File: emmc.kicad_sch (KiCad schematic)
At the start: 16 parts, among them U22 HN8T05DEHK-X073

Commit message: Add files via upload
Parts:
- C320: renamed from C121; value 100n -> 1u
- C321: renamed from C122; value 100n -> 1u
- C322: renamed from C123; value 100n -> 1u
- C324: renamed from C129; value 100n -> 1u
- C325: renamed from C130; value 100n -> 1u
- C326: renamed from C131; value 100n -> 1u
- C331: renamed from C125; value 100n -> 1u
- C332: renamed from C126; value 100n -> 1u
- C333: renamed from C127; value 100n -> 1u
- renumbered C120 to C319, C128 to C323, C132 to C327, C133 to C328, C134 to C329, C124 to C330, U22 to U24
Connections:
- net +1.8V: no longer U24.A6 (VCCQ2), U24.A7 (VCCQ2), U24.B6 (VCCQ2), U24.B7 (VCCQ2), U24.C6 (VCCQ2), U24.C7 (VCCQ2), U24.K6 (VCCQ2), U24.K7 (VCCQ2)
- new net VCCQ2: U24.A6 (VCCQ2), U24.A7 (VCCQ2), U24.B6 (VCCQ2), U24.B7 (VCCQ2), U24.C6 (VCCQ2), U24.C7 (VCCQ2), U24.K6 (VCCQ2), U24.K7 (VCCQ2)
- no-connect marks 14 -> 15
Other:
- note added: "I NEED 2.5V & 1.2V"

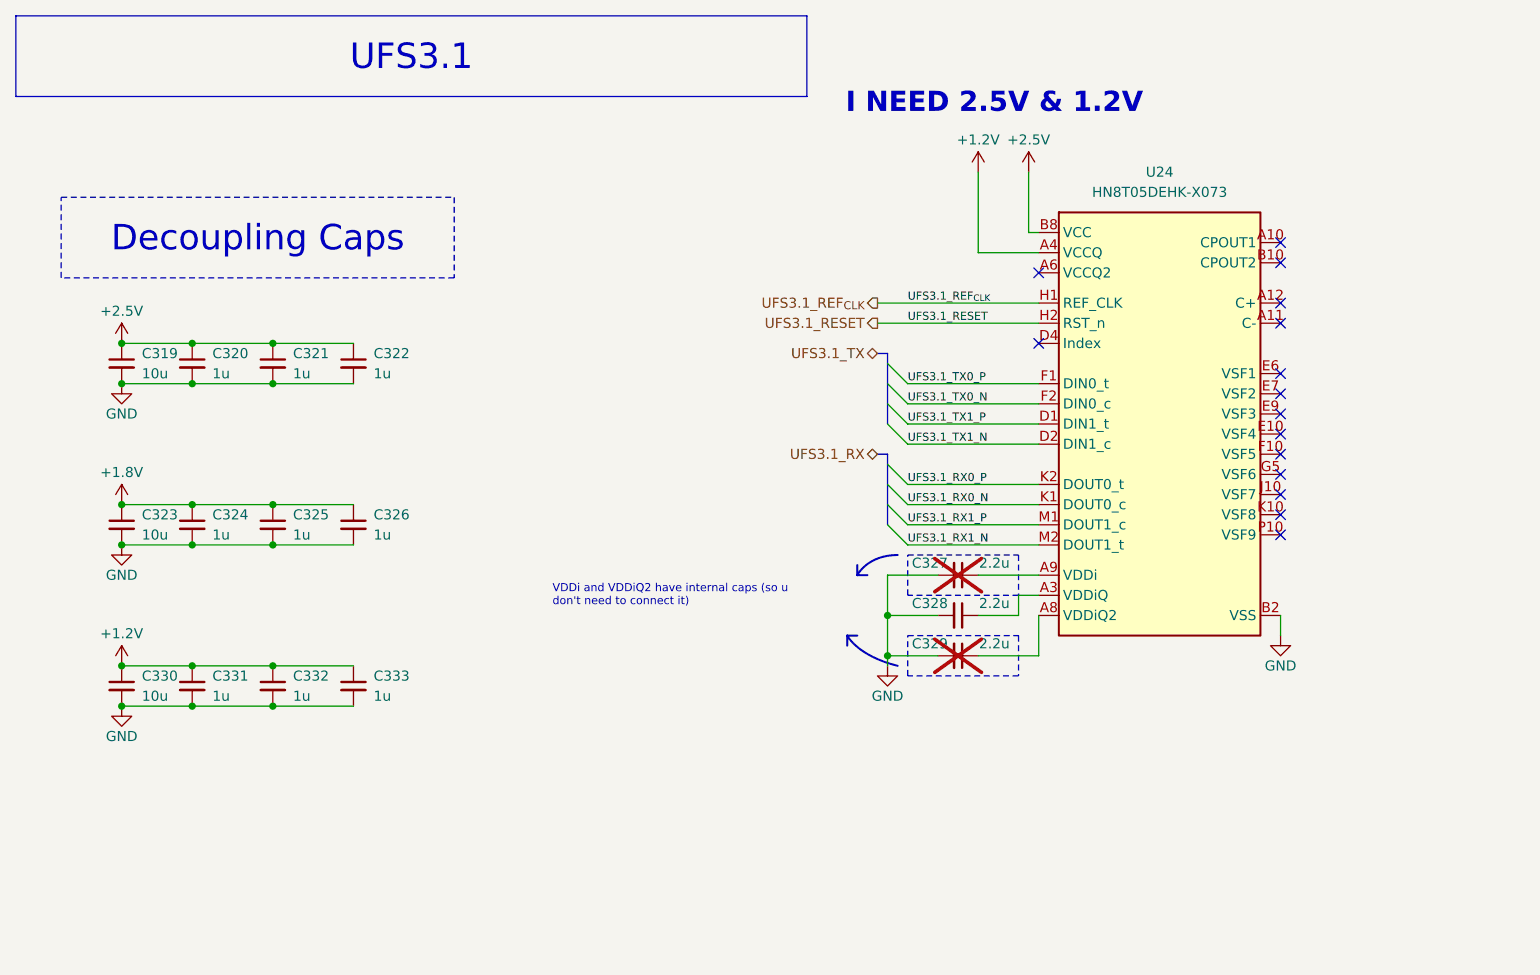
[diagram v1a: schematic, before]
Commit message: SBC Board V0.2
The SBC schematics before footprint and part number check
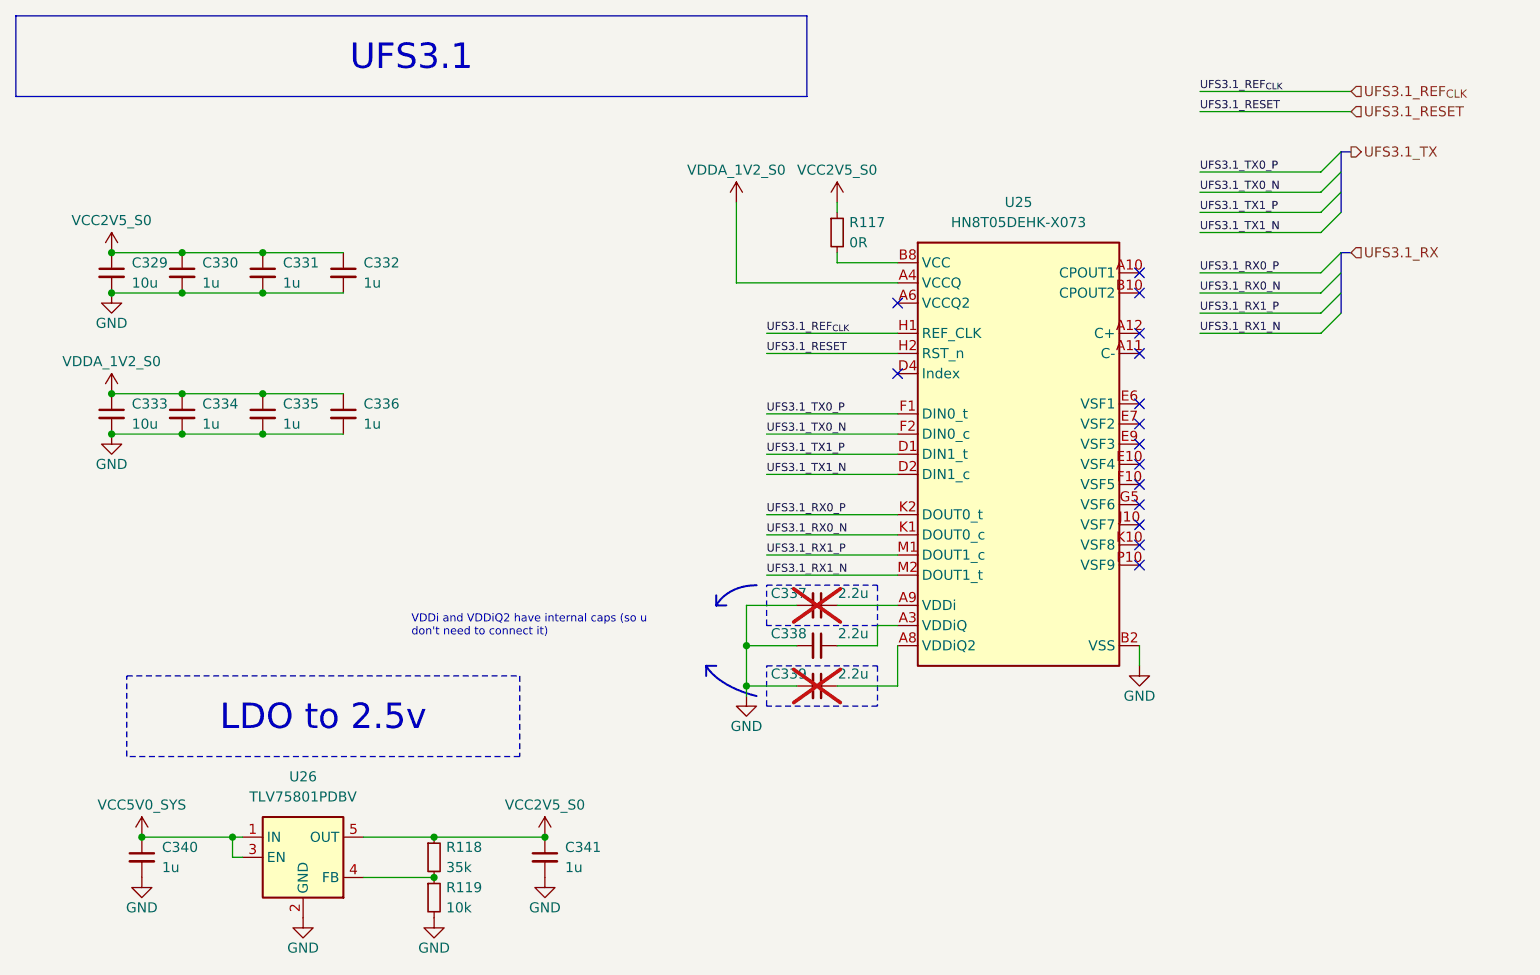
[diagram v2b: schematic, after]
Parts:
- removed C323: 10u, Capacitor_SMD:C_0402_1005Metric, symbol New_Library_0:C_Small_edited
- removed C324, C325, C326: 1u, Capacitor_SMD:C_0201_0603Metric_Pad0.64x0.40mm_HandSolder, symbol New_Library_0:C_Small_edited
- added C340, C341: 1u, Capacitor_SMD:C_0201_0603Metric_Pad0.64x0.40mm_HandSolder, symbol New_Library_0:C_Small_edited
- added R117: 0R, PCM_Resistor_SMD_AKL:R_0402_1005Metric, symbol Device:R_Small
- added R118: 35k, PCM_Resistor_SMD_AKL:R_0402_1005Metric, symbol Device:R_Small
- added R119: 10k, PCM_Resistor_SMD_AKL:R_0402_1005Metric, symbol Device:R_Small
- added U26: TLV75801PDBV, Package_TO_SOT_SMD:SOT-23-5, symbol Regulator_Linear:TLV75801PDBV
- renumbered C319 to C329, C320 to C330, C321 to C331, C322 to C332, C330 to C333, C331 to C334, C332 to C335, C333 to C336, C327 to C337, C328 to C338, C329 to C339, U24 to U25
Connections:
- net GND: now also C340.2, C341.2, R119.2, U26.2 (GND)
- net +1.2V renamed VCCQ
- net +2.5V renamed VCC
- net VCC: now also R117.2; no longer C329.1, C330.1, C331.1, C332.1
- new net: R118.2, R119.1, U26.4 (FB)
- new net VCC2V5_S0: C329.1, C330.1, C331.1, C332.1, C341.1, R117.1, R118.1, U26.5 (OUT)
- new net VCC5V0_SYS: C340.1, U26.1 (IN), U26.3 (EN)
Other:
- note removed: "I NEED 2.5V & 1.2V"
- moved on the sheet: C329, C330, C331, C332, C333, C334, C335, C336, C337, C338, C339, U25

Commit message: SBCv0.3
there is no big thing update just some LCSC & Mouser parts
and Big problem deleted alot of component values (:
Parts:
- removed C329, C333: 10u, Capacitor_SMD:C_0402_1005Metric, symbol New_Library_0:C_Small_edited
- added C214, C283: 10u, Capacitor_SMD:C_0603_1608Metric, symbol New_Library_0:C_Small_edited
- C330, C331, C332, C334, C335, C336, C340, C341: LCSC Part (none) -> C5209398; Mouser Part (none) -> CL03A105KP3NSNC
- C337, C338, C339: LCSC Part (none) -> C170151; Mouser Part (none) -> 187-CL05A225KO5NQNC
- R117: value 0R -> (none); LCSC Part (none) -> (effects
- R118: value 35k -> (none); LCSC Part (none) -> (hide yes)
- R119: LCSC Part (none) -> (at 0 0 0)
- U25: value HN8T05DEHK-X073 -> (none); LCSC Part (none) -> (pin passive line
- U26: value TLV75801PDBV -> (none); Mouser Part (none) -> (at 0 2.54 270)
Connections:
- net GND: now also C214.2, C283.2
- net VCC2V5_S0: now also C214.1
- net VCCQ: now also C283.1

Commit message: SBCv0.4
add LCSC & Mouser parts 
and solve the deleted value in the past version
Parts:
- removed R117, R118: (no value), PCM_Resistor_SMD_AKL:R_0402_1005Metric, symbol Device:R_Small
- removed R119: 10k, PCM_Resistor_SMD_AKL:R_0402_1005Metric, symbol Device:R_Small
- removed U26: (no value), Package_TO_SOT_SMD:SOT-23-5, symbol Regulator_Linear:TLV75801PDBV
- added R238: 35k, PCM_Resistor_SMD_AKL:R_0402_1005Metric, symbol Device:R_Small
- added R239: 10k, PCM_Resistor_SMD_AKL:R_0402_1005Metric, symbol Device:R_Small
- added R240: 0R, PCM_Resistor_SMD_AKL:R_0402_1005Metric, symbol Device:R_Small
- added U52: TLV75801PDBVR, Package_TO_SOT_SMD:SOT-23-5, symbol Regulator_Linear:TLV75801PDBV
- U25: value (none) -> HN8T05DEHK-X073; LCSC Part (pin passive line -> (none)
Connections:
- net GND: now also R239.2, U52.2 (GND)
- net VCC: now also R240.2
- net VCC2V5_S0: now also R238.1, R240.1, U52.5 (OUT)
- net VCC5V0_SYS: now also U52.1 (IN), U52.3 (EN)
- new net: R238.2, R239.1, U52.4 (FB)
